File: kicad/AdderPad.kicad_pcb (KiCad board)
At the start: 2 copper layers, 114.3 x 39.7 mm, 18 parts, among them SW1 SW_Push, U1 ProMicro

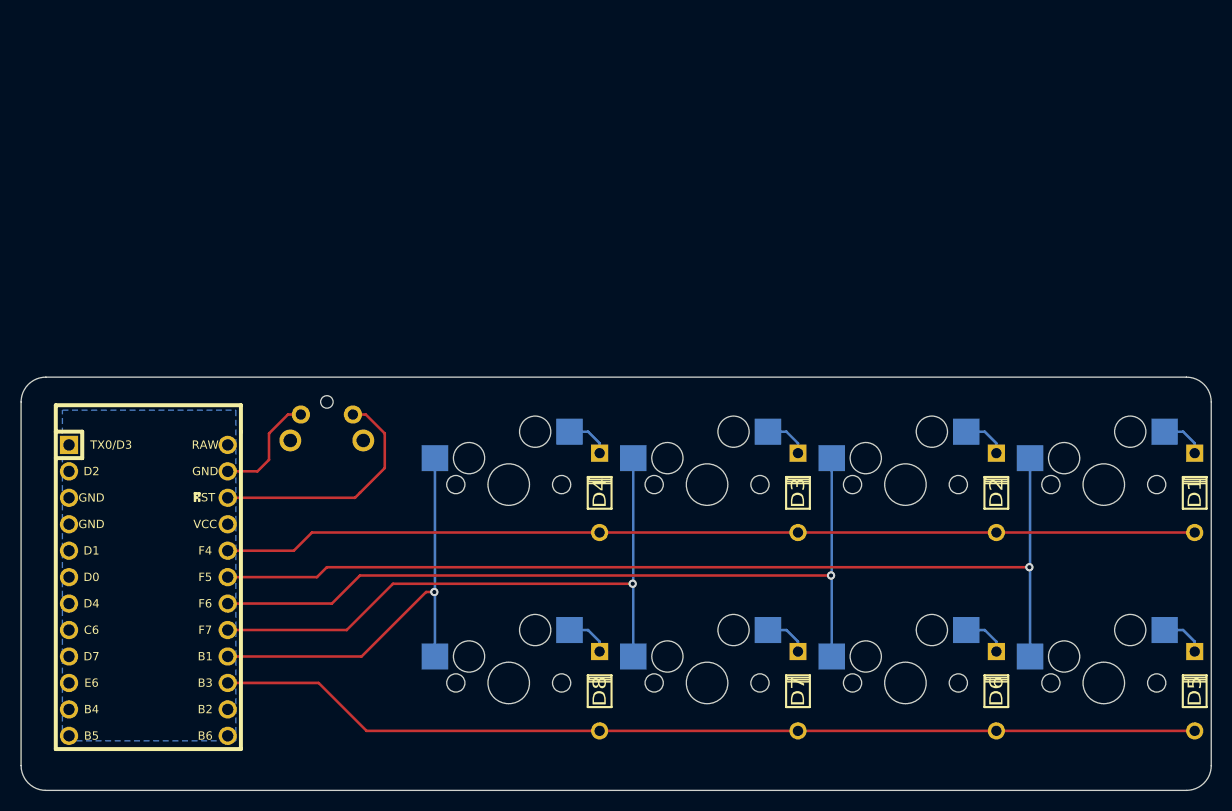
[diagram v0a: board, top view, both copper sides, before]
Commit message: Added RGB underglow LEDs
Rerouted traces, new mill sizes
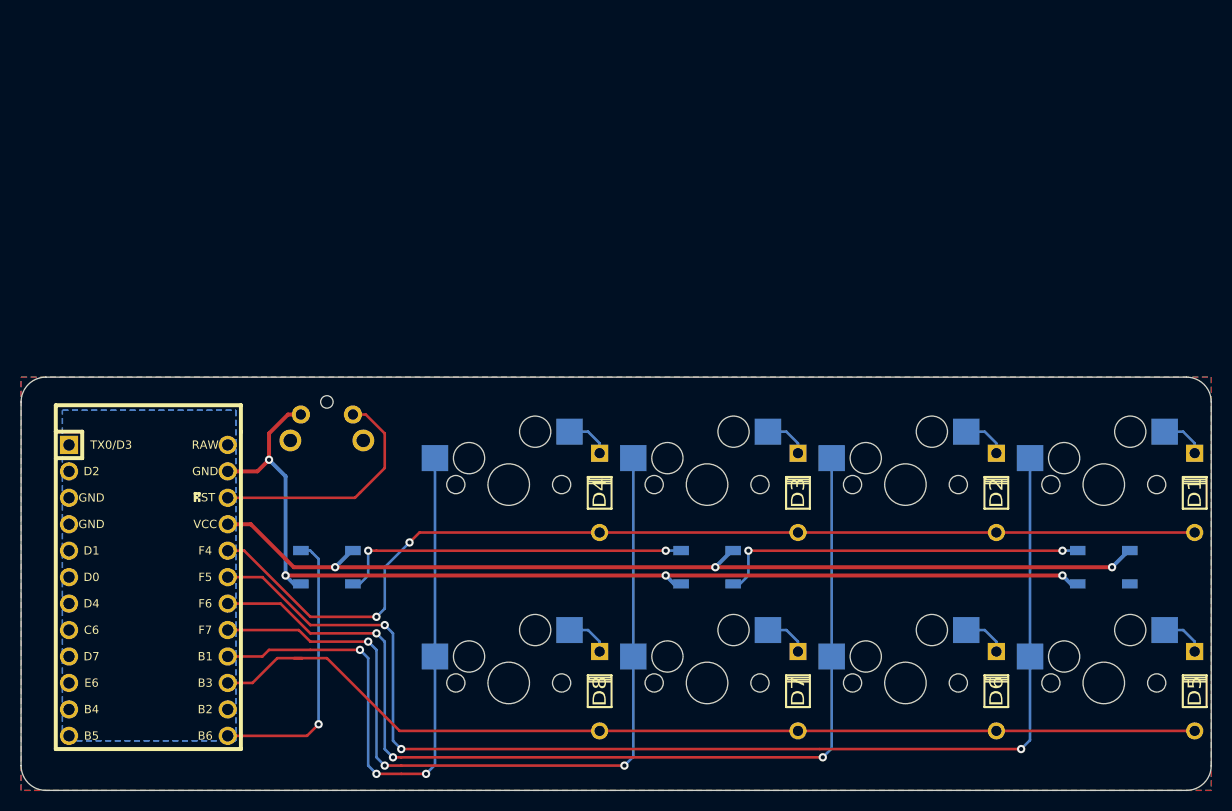
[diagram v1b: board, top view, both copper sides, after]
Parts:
- added RGB1: WS2812B, Keebio-Parts:WS2812B, B.Cu at (123.8, 128.6)
- added RGB2: WS2812B, Keebio-Parts:WS2812B, B.Cu at (160.3, 128.6)
- added RGB3: WS2812B, Keebio-Parts:WS2812B, B.Cu at (198.4, 128.6)
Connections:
- U1 pad 13: Net-(U1-Pad13) -> LED
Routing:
- net VCC: track 0.00 -> 93.7 mm, vias 0 -> 3
- net GND: track 10.8 -> 102.6 mm, vias 0 -> 4
- net Net-(RGB2-Pad2): track 0.00 -> 35.8 mm, vias 0 -> 2
- net Net-(RGB1-Pad2): track 0.00 -> 34.2 mm, vias 0 -> 2
- net LED: track 0.00 -> 27.1 mm, vias 0 -> 1
- net COL0: track 96.5 -> 117.4 mm, vias 1 -> 3
- net COL1: track 78.2 -> 98.4 mm, vias 1 -> 3
- net COL2: track 59.9 -> 79.4 mm, vias 1 -> 3
- net COL3: track 41.5 -> 61.0 mm, vias 1 -> 3
- net ROW0: track 93.6 -> 101.2 mm, vias 0 -> 2
- net ROW1: track 94.8 -> 97.5 mm
- added copper zone on B.Cu, net (none)
- added copper zone on F.Cu, net (none)
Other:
- net class Default: trace_width 0.25 -> 0.254
- net class Power added: clearance 0.2, trace_width 0.381, via_dia 0.8, via_drill 0.4

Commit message: Multiple updates
- added 128x64 OLED support
- added fourth underglow RGB
- resize PCB
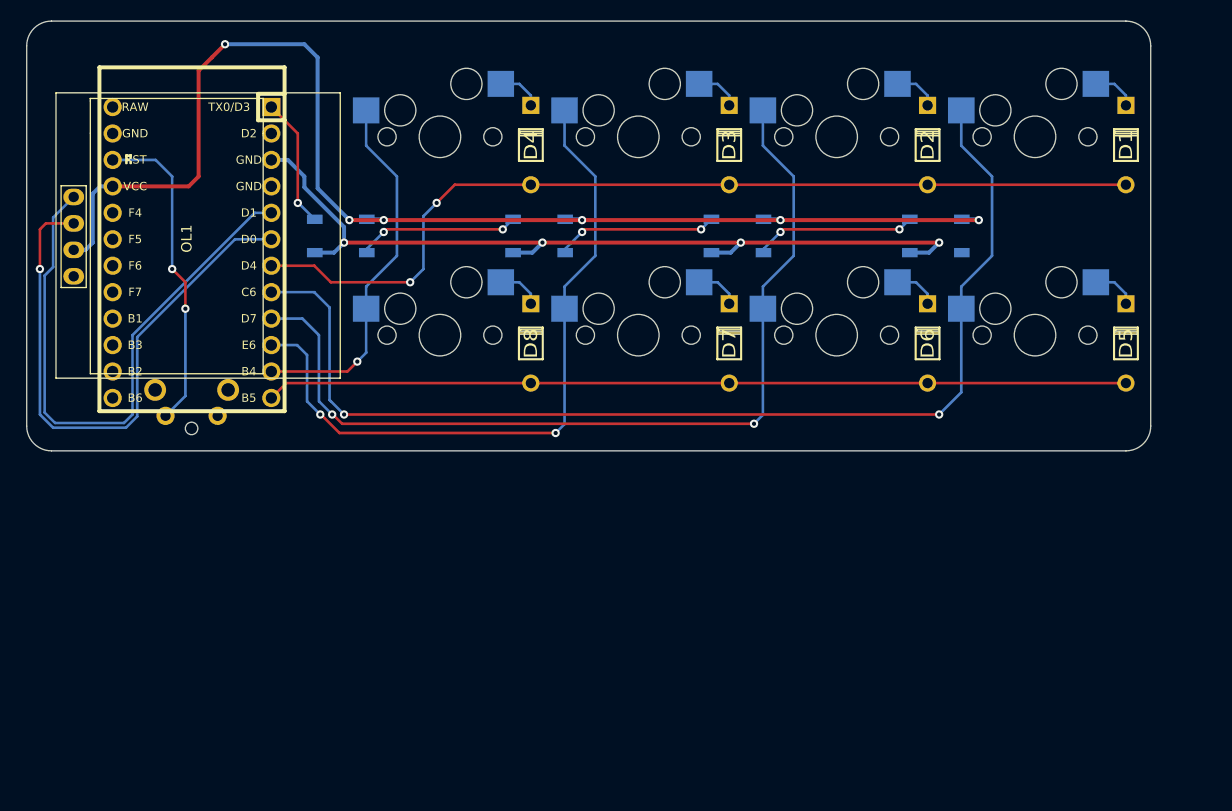
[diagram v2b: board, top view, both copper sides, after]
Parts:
- added OL1: SSD1306, SSD1306:128x64OLED, F.Cu at (110.1, 97.0)
- added RGB4: WS2812B, Keebio-Parts:WS2812B, B.Cu at (182.3, 96.8)
- U1: moved to B.Cu
- moved RGB3 47.4 mm to (163.3, 96.8)
- moved RGB2 35.7 mm to (144.2, 96.8)
- moved D5 34.0 mm to (200.6, 107.1)
- moved D6 34.0 mm to (181.5, 107.1)
- moved D7 34.0 mm to (162.5, 107.1)
- moved D8 34.0 mm to (143.4, 107.1)
- moved MX1 34.0 mm to (191.8, 87.2)
- moved MX2 34.0 mm to (172.8, 87.2)
- moved MX3 34.0 mm to (153.7, 87.2)
- moved MX4 34.0 mm to (134.7, 87.2)
- moved D1 34.0 mm to (200.6, 88.0)
- moved D2 34.0 mm to (181.5, 88.0)
- moved D3 34.0 mm to (162.5, 88.0)
- moved D4 34.0 mm to (143.4, 88.0)
- moved MX5 34.0 mm to (191.8, 106.3)
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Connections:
- U1 pad 1: Net-(U1-Pad1) -> LED
- U1 pad 10: Net-(U1-Pad10) -> COL2
- U1 pad 11: Net-(U1-Pad11) -> COL3
- U1 pad 12: Net-(U1-Pad12) -> ROW1
- U1 pad 13: LED -> Net-(U1-Pad13)
- U1 pad 15: ROW1 -> Net-(U1-Pad15)
- U1 pad 16: COL3 -> Net-(U1-Pad16)
- U1 pad 17: COL2 -> Net-(U1-Pad17)
- U1 pad 18: COL1 -> Net-(U1-Pad18)
- U1 pad 19: COL0 -> Net-(U1-Pad19)
- U1 pad 20: ROW0 -> Net-(U1-Pad20)
- U1 pad 5: Net-(U1-Pad5) -> SDA
- U1 pad 6: Net-(U1-Pad6) -> SCL
- U1 pad 7: Net-(U1-Pad7) -> ROW0
- U1 pad 8: Net-(U1-Pad8) -> COL0
- U1 pad 9: Net-(U1-Pad9) -> COL1
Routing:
- net SDA: track 0.00 -> 57.6 mm
- net SCL: track 0.00 -> 56.1 mm, vias 0 -> 1
- net VCC: track 93.7 -> 124.8 mm, vias 3 -> 6
- net COL3: track 61.0 -> 35.6 mm, vias 3 -> 1
- net GND: track 102.6 -> 81.8 mm
- net Net-(RGB2-Pad2): track 35.8 -> 15.6 mm
- net Net-(RGB1-Pad2): track 34.2 -> 15.6 mm
- net Net-(RGB3-Pad2): track 0.00 -> 15.6 mm, vias 0 -> 2
- net ROW1: track 97.5 -> 82.7 mm
- net LED: track 27.1 -> 12.5 mm
- net COL2: track 79.4 -> 67.2 mm, vias 3 -> 2
- net ROW0: track 101.2 -> 89.6 mm
- net COL1: track 98.4 -> 87.2 mm, vias 3 -> 2
- net COL0: track 117.4 -> 106.7 mm, vias 3 -> 2
- net reset: track 23.4 -> 30.7 mm, vias 0 -> 2
- removed copper zone on B.Cu, net (none)
- removed copper zone on F.Cu, net (none)
- removed copper zone on B.Cu, net GND
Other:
- board size 114.3 x 39.7 mm -> 108 x 41.3 mm
- board text added: "GND"
- board text added: "SCL"
- board text added: "SDA"
- board text added: "VCC"

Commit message: Repositioned
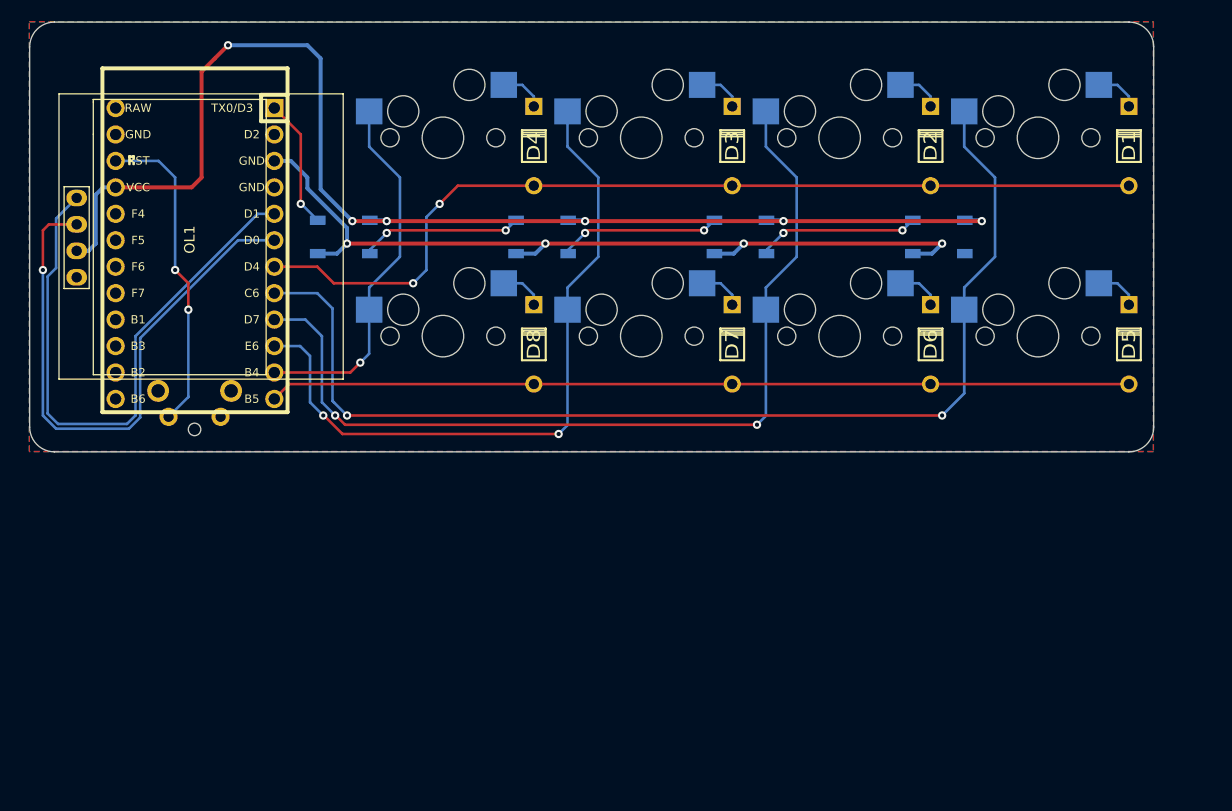
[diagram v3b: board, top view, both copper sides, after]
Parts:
- moved D1 0.30 mm to (200.9, 88.1)
- moved D2 0.30 mm to (181.8, 88.1)
- moved D4 0.30 mm to (143.7, 88.1)
- moved D5 0.30 mm to (200.9, 107.2)
- moved D6 0.30 mm to (181.8, 107.2)
- moved D8 0.30 mm to (143.7, 107.2)
- moved MX1 0.30 mm to (192.1, 87.3)
- moved MX2 0.30 mm to (173.1, 87.3)
- moved MX3 0.30 mm to (154.0, 87.3)
- moved MX5 0.30 mm to (192.1, 106.4)
- moved MX6 0.30 mm to (173.1, 106.4)
- moved MX7 0.30 mm to (154.0, 106.4)
- moved OL1 0.30 mm to (110.4, 97.1)
- moved RGB2 0.30 mm to (144.5, 96.9)
- moved RGB3 0.30 mm to (163.5, 96.9)
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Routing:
- added copper zone on B.Cu, net GND
- added copper zone on F.Cu, net GND
